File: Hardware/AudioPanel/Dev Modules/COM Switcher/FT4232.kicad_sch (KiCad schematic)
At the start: 81 parts, among them J601 2.54mm, J602 PC1_COM, J603 PC2_COM, J604 PC3_COM, J605 PC4_COM, Q601 BCM857BS, U601 FT4232H, U602 93LCxxA, Y601 12MHz

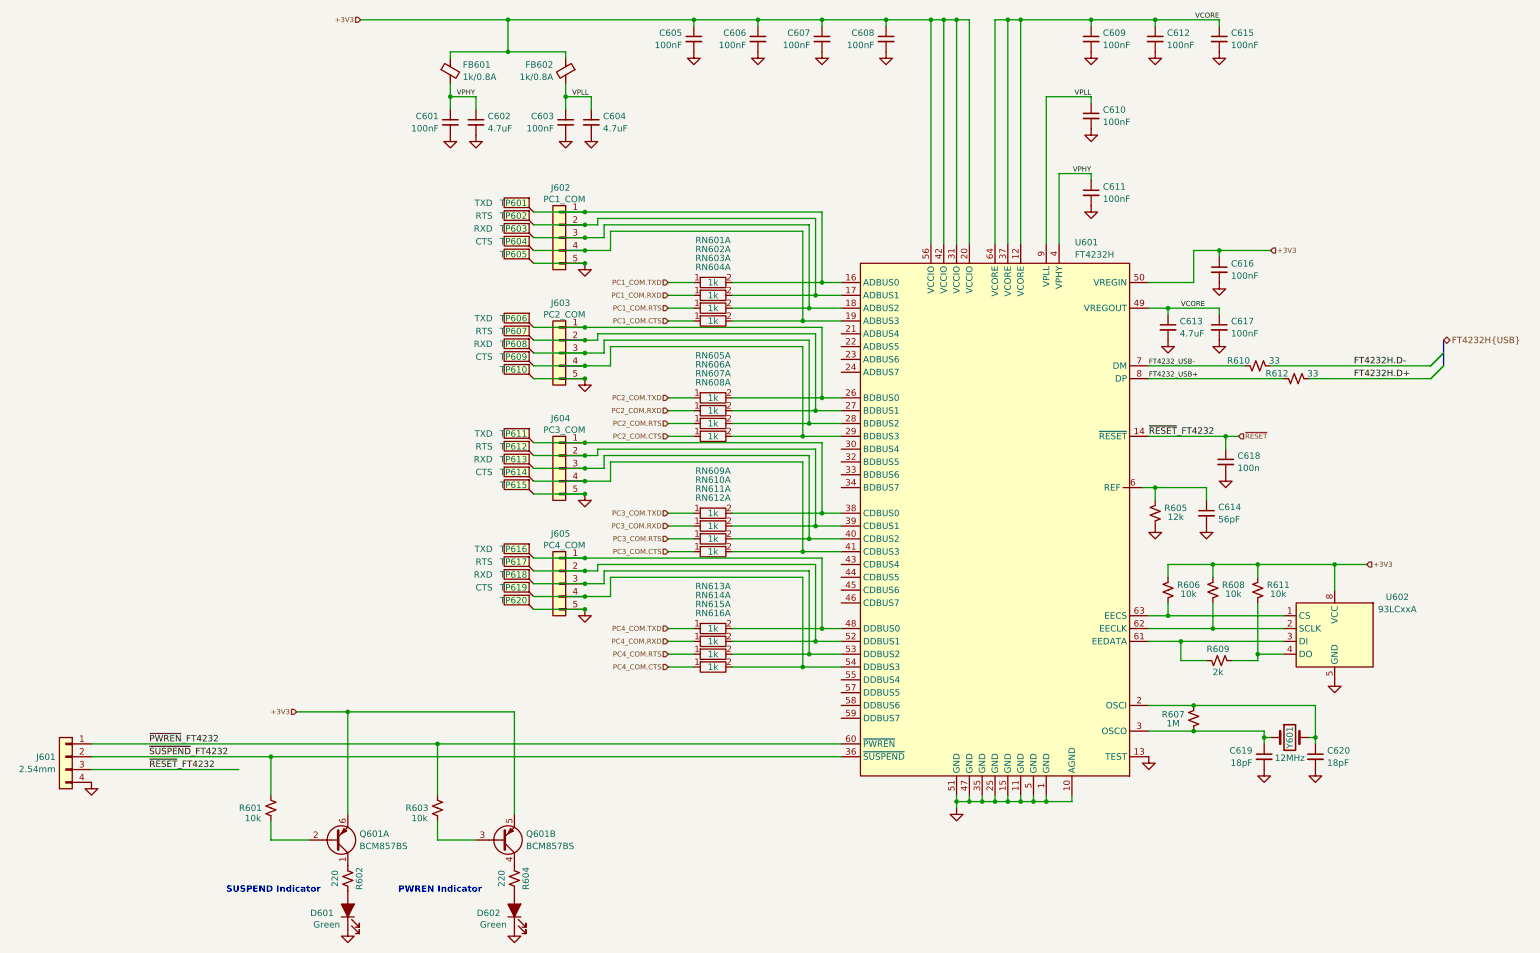
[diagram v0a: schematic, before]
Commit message: Added level shifters for all SAMD21s
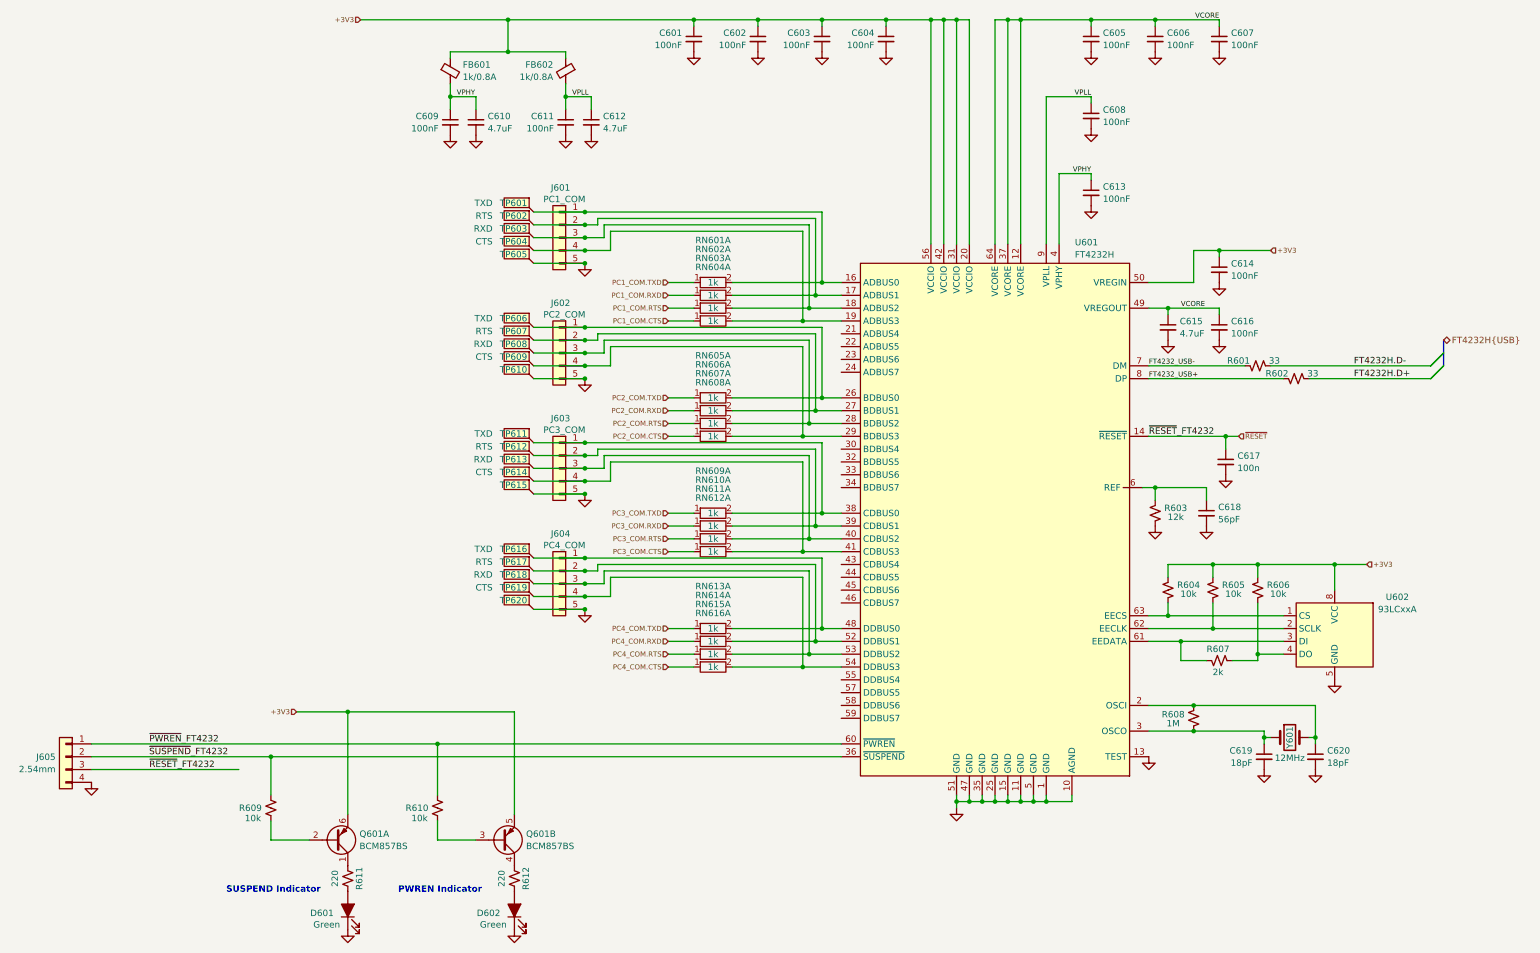
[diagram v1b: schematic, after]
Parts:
- renumbered C605 to C601, C606 to C602, C607 to C603, C608 to C604, C609 to C605, C612 to C606, C615 to C607, C610 to C608, C601 to C609, C602 to C610, C603 to C611, C604 to C612, C611 to C613, C616 to C614, C613 to C615, C617 to C616, C618 to C617, C614 to C618, J602 to J601, J603 to J602, J604 to J603, J605 to J604, J601 to J605, R610 to R601, R612 to R602, R605 to R603, R606 to R604, R608 to R605, R611 to R606, R609 to R607, R607 to R608, R601 to R609, R603 to R610, R602 to R611, R604 to R612

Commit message: Added footprints for the missing
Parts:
- J601, J602, J603, J604: footprint Connector_JST:JST_PH_S6B-PH-K_1x06_P2.00mm_Horizontal -> Connector_PinHeader_2.54mm:PinHeader_1x05_P2.54mm_Vertical
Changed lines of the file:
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@@
 			)
 		)
-		(property "Footprint" "Connector_JST:JST_PH_S6B-PH-K_1x06_P2.00mm_Horizontal"
+		(property "Footprint" "Connector_PinHeader_2.54mm:PinHeader_1x05_P2.54mm_Vertical"
 			(at 191.77 144.78 0)
 			(effects
@@
 			)
 		)
-		(property "Footprint" "Connector_JST:JST_PH_S6B-PH-K_1x06_P2.00mm_Horizontal"
+		(property "Footprint" "Connector_PinHeader_2.54mm:PinHeader_1x05_P2.54mm_Vertical"
 			(at 191.77 121.92 0)
 			(effects
@@
 			)
 		)
-		(property "Footprint" "Connector_JST:JST_PH_S6B-PH-K_1x06_P2.00mm_Horizontal"
+		(property "Footprint" "Connector_PinHeader_2.54mm:PinHeader_1x05_P2.54mm_Vertical"
 			(at 191.77 99.06 0)
 			(effects
@@
 			)
 		)
-		(property "Footprint" "Connector_JST:JST_PH_S6B-PH-K_1x06_P2.00mm_Horizontal"
+		(property "Footprint" "Connector_PinHeader_2.54mm:PinHeader_1x05_P2.54mm_Vertical"
 			(at 191.77 76.2 0)
 			(effects

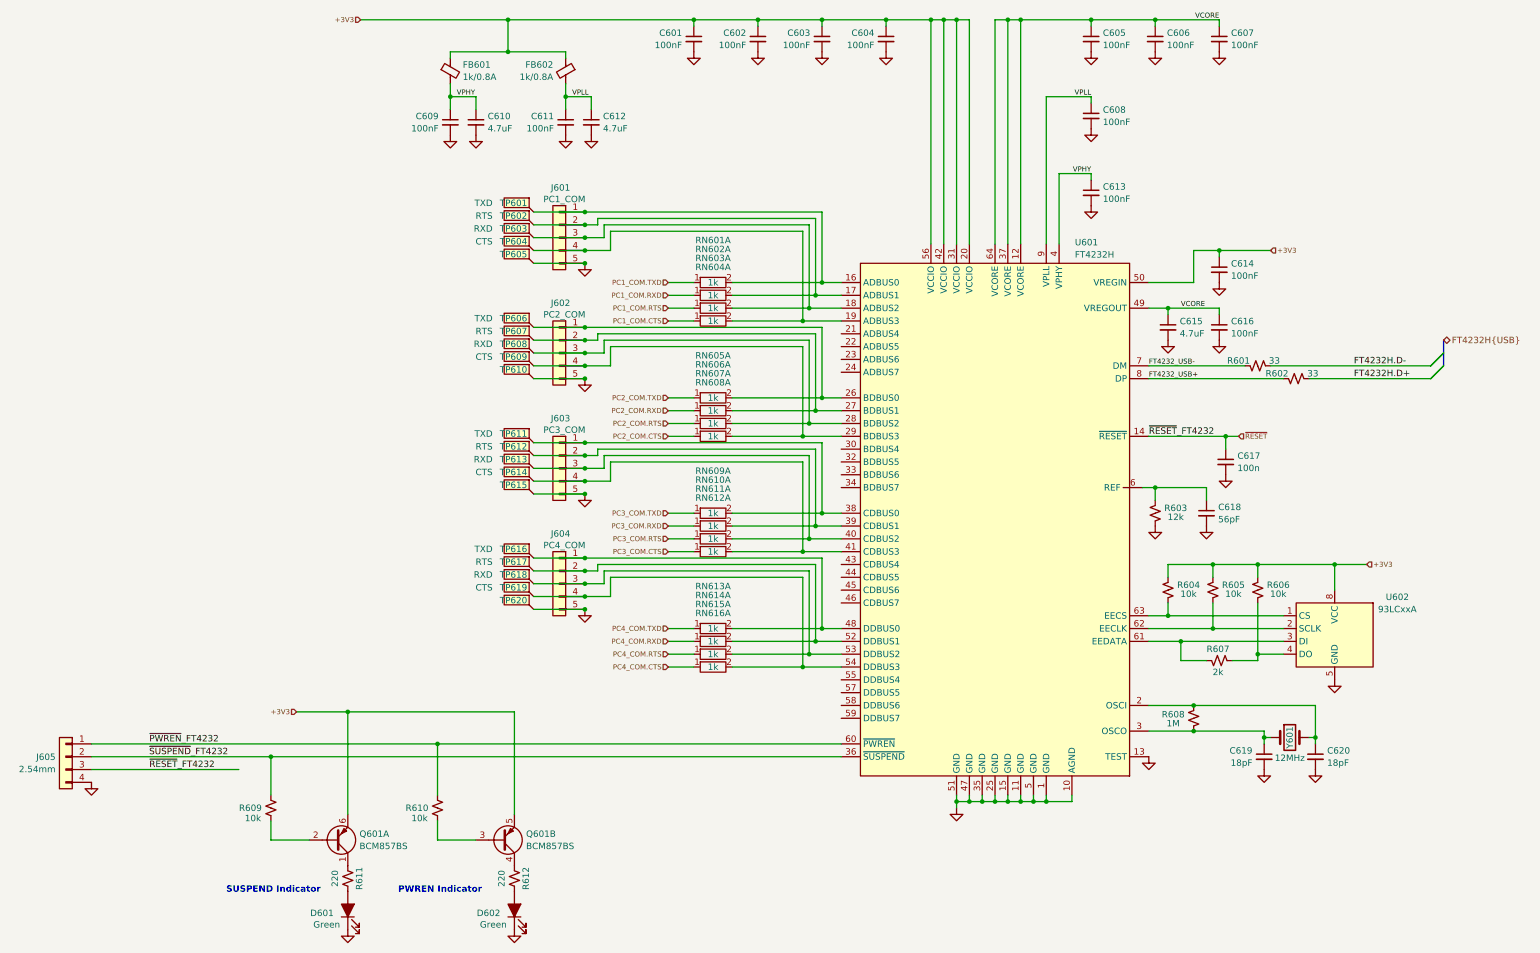
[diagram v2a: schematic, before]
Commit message: Changed DB9 connectors to stacked
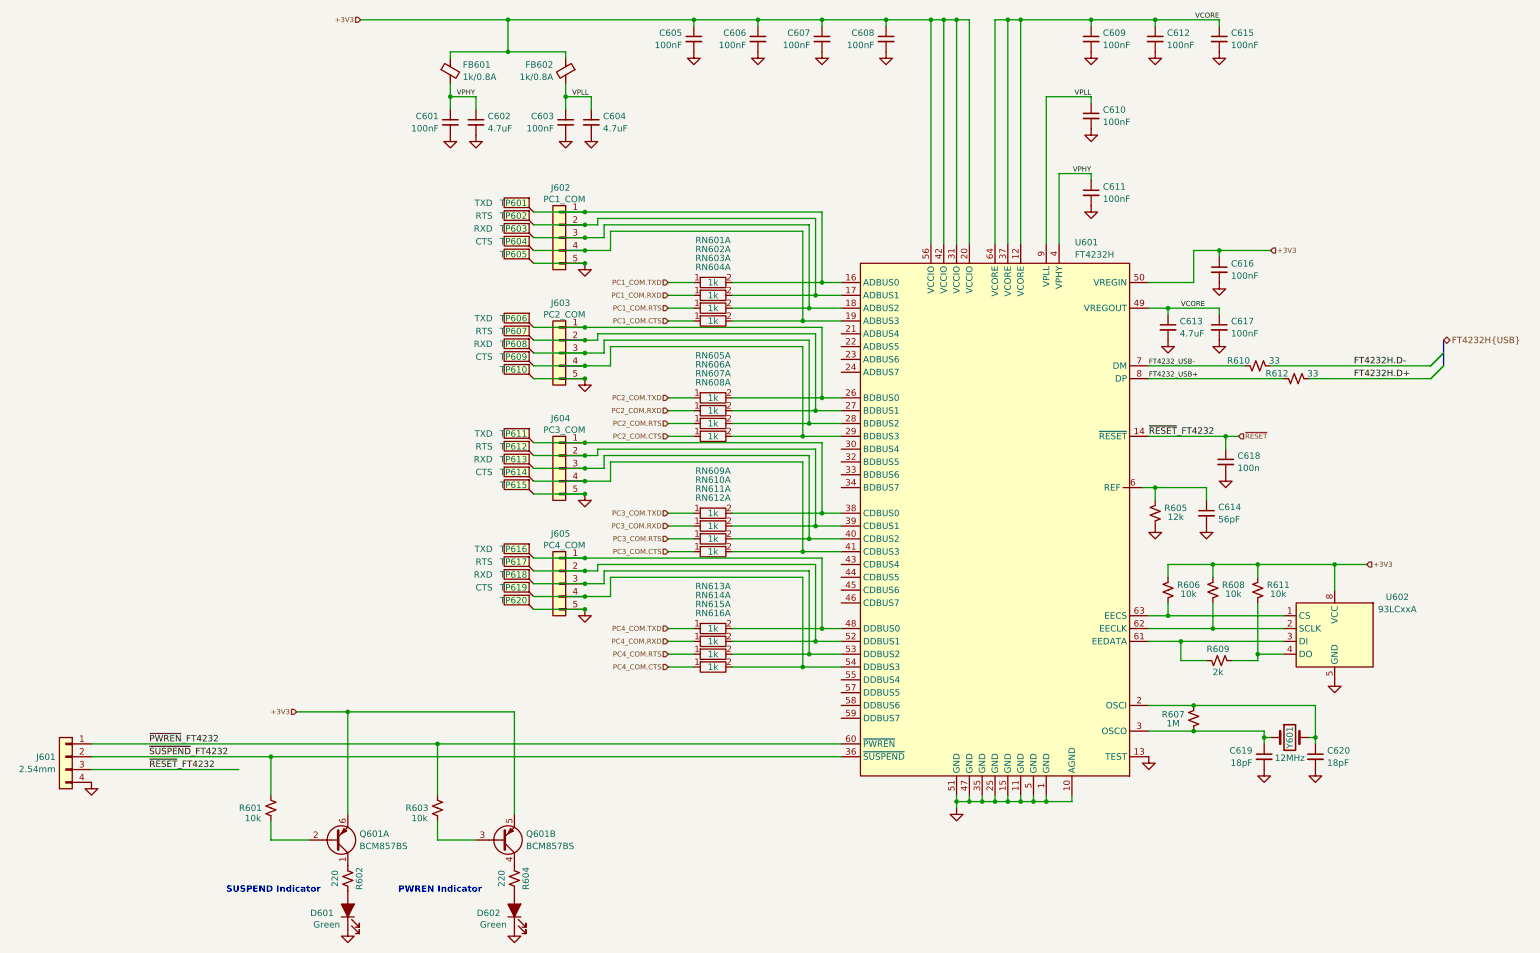
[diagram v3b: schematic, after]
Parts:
- renumbered C609 to C601, C610 to C602, C611 to C603, C612 to C604, C601 to C605, C602 to C606, C603 to C607, C604 to C608, C605 to C609, C608 to C610, C613 to C611, C606 to C612, C615 to C613, C618 to C614, C607 to C615, C614 to C616, C616 to C617, C617 to C618, J605 to J601, J601 to J602, J602 to J603, J603 to J604, J604 to J605, R609 to R601, R611 to R602, R610 to R603, R612 to R604, R603 to R605, R604 to R606, R608 to R607, R605 to R608, R607 to R609, R601 to R610, R606 to R611, R602 to R612

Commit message: Fixed I2C pullups to 3V3
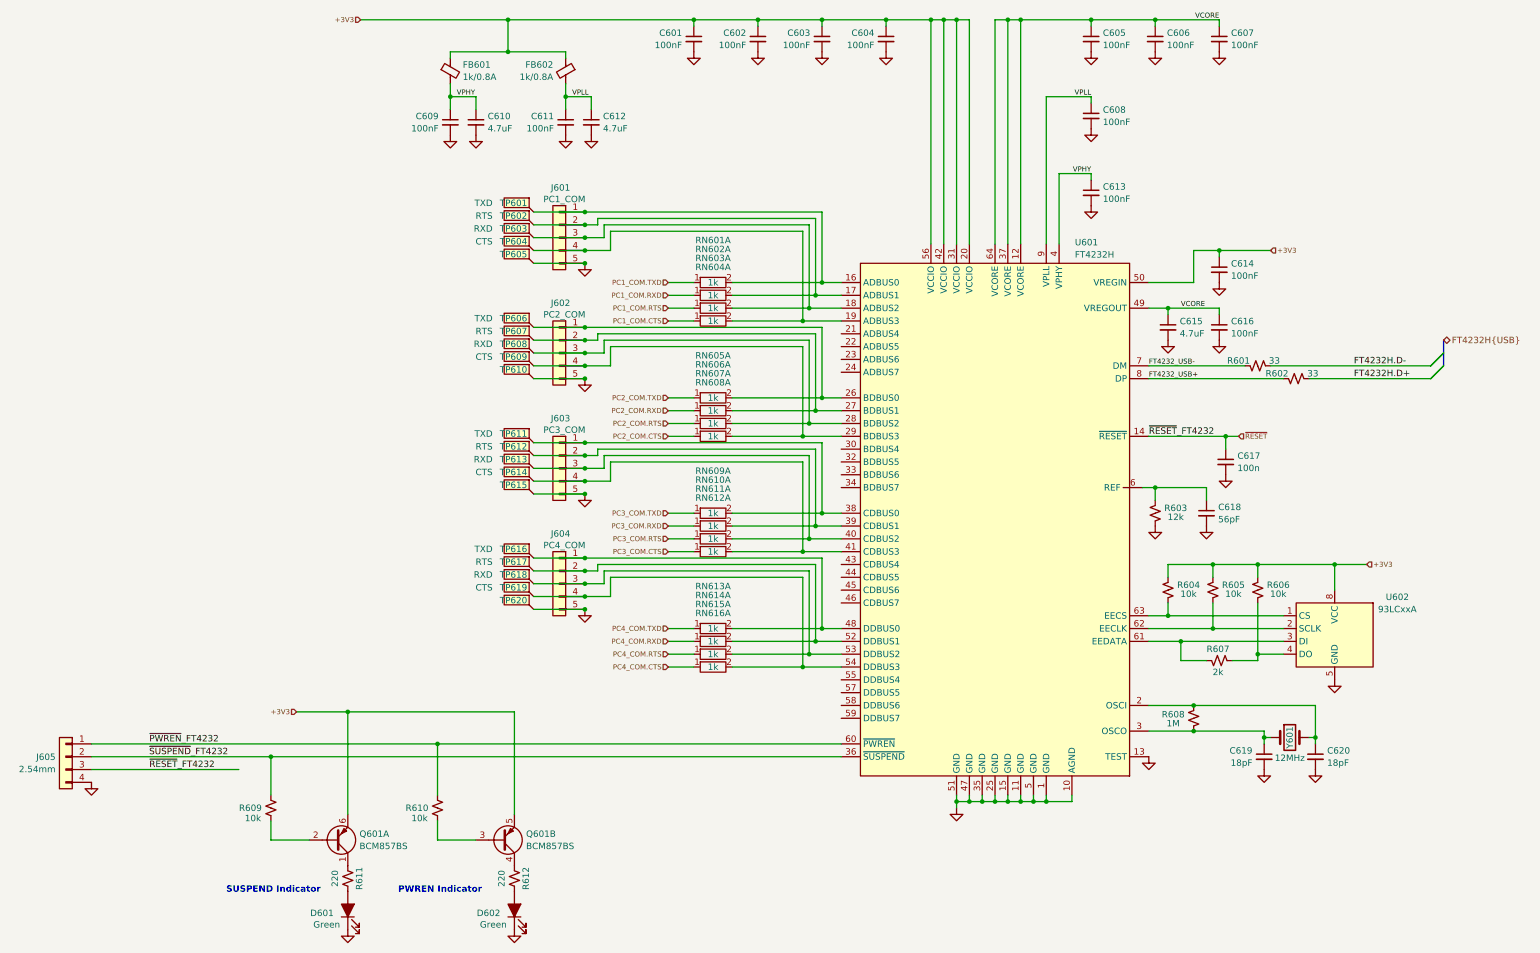
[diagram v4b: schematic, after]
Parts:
- renumbered C605 to C601, C606 to C602, C607 to C603, C608 to C604, C609 to C605, C612 to C606, C615 to C607, C610 to C608, C601 to C609, C602 to C610, C603 to C611, C604 to C612, C611 to C613, C616 to C614, C613 to C615, C617 to C616, C618 to C617, C614 to C618, J602 to J601, J603 to J602, J604 to J603, J605 to J604, J601 to J605, R610 to R601, R612 to R602, R605 to R603, R606 to R604, R608 to R605, R611 to R606, R609 to R607, R607 to R608, R601 to R609, R603 to R610, R602 to R611, R604 to R612
